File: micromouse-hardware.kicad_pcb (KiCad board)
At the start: 2 copper layers, 85 x 103.5 mm, 56 parts, among them J1 BATT-CONN, Q1 BCP56, Q10 BCP56, Q2 BCP56, Q3 BCP56, Q4 TEFT4300, Q5 TEFT4300, Q6 TEFT4300, Q7 TEFT4300, Q8 TEFT4300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

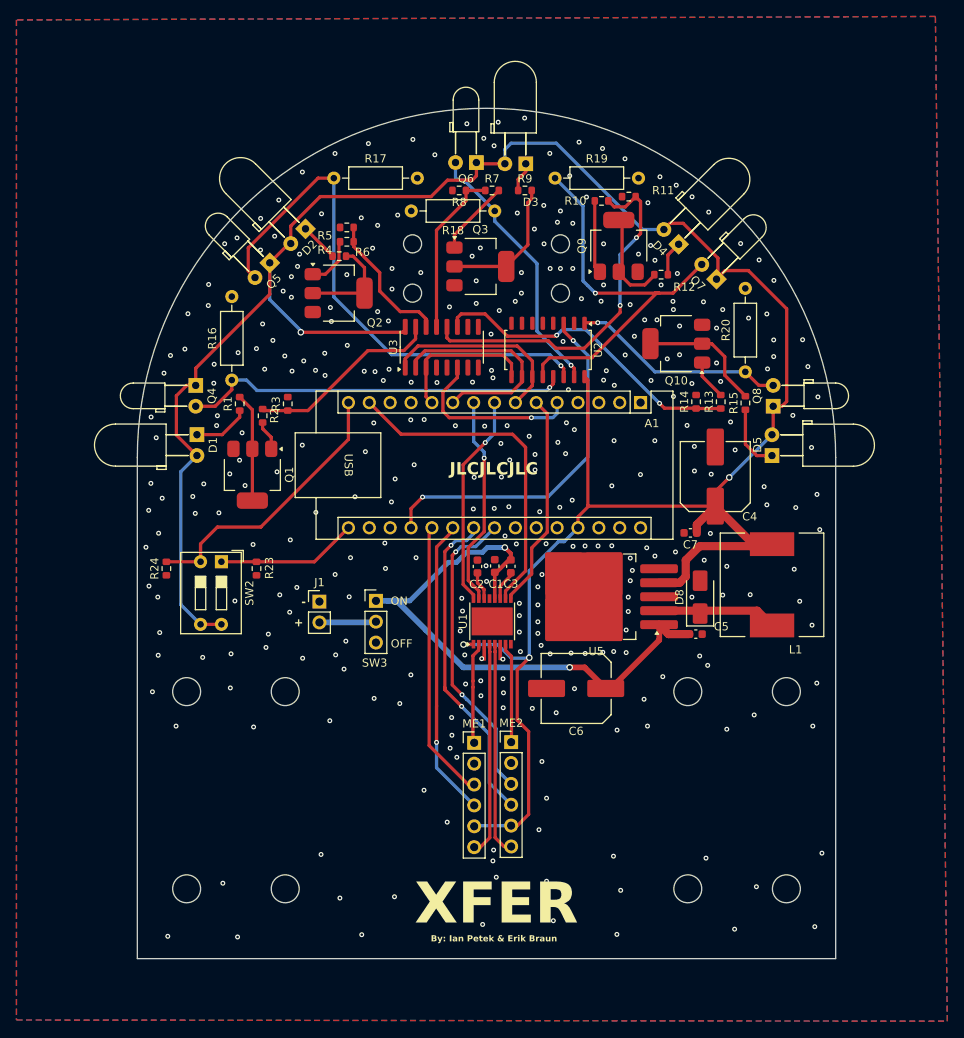
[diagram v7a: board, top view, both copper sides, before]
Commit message: promjenio tranistore u mosfete, jos neki popravci
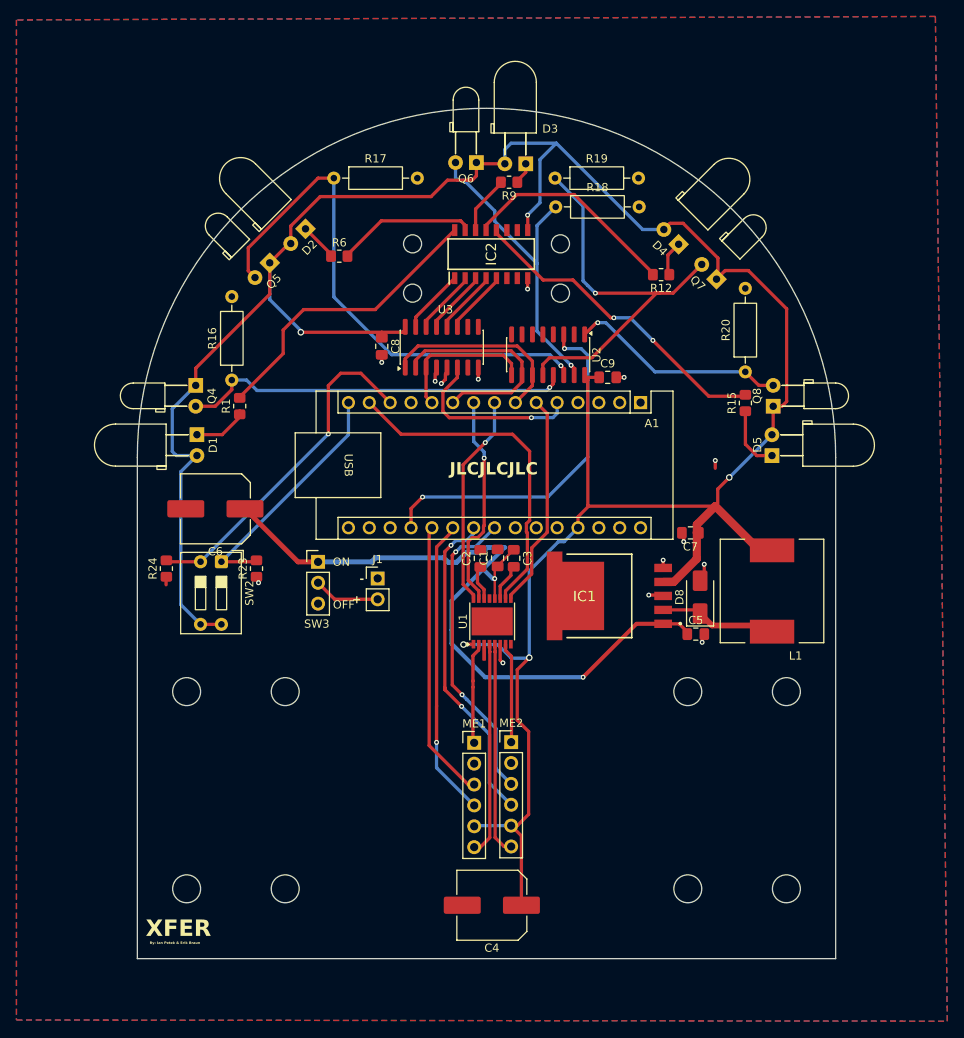
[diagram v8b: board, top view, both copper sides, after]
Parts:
- removed Q1, Q10, Q2, Q3, Q9: BCP56, Custom:SOT-223-3_TabPin4
- removed R10, R13, R2, R4, R7: 820R, Resistor_SMD:R_0603_1608Metric
- removed R11, R14, R3, R5, R8: 10K, Resistor_SMD:R_0603_1608Metric
- removed U5: LM2575GR-5.0, Package_TO_SOT_SMD:TO-263-5_TabPin3
- added C8: 100nF, Capacitor_SMD:C_0805_2012Metric_Pad1.18x1.45mm_HandSolder, F.Cu at (137.2, 73.5)
- added C9: 100nF, Capacitor_SMD:C_0805_2012Metric_Pad1.18x1.45mm_HandSolder, F.Cu at (164.8, 77.2)
- added IC1: LM2575SX-5.0_NOPB, Custom:KTT0005B, F.Cu at (159.0, 103.8)
- added IC2: TBD62003AFG,EL, Custom:SOIC127P630X190-16N, F.Cu at (150.6, 62.2)
- C1, C2, C3, C5, C7: footprint Capacitor_SMD:C_0603_1608Metric -> Capacitor_SMD:C_0805_2012Metric_Pad1.18x1.45mm_HandSolder
- D1, D2, D3, D4, D5: value SHF4545 -> SFH4545
- R1, R12, R15, R23, R24, R6, R9: footprint Resistor_SMD:R_0603_1608Metric -> Resistor_SMD:R_0805_2012Metric_Pad1.20x1.40mm_HandSolder
- U2: footprint Package_SO:SOIC-16_4.55x10.3mm_P1.27mm -> Package_SO:SOIC-16_3.9x9.9mm_P1.27mm
- moved C4 58.8 mm to (150.7, 141.5), turned to 180 degrees
- moved C6 49.1 mm to (117.0, 93.2)
- moved SW3 8.49 mm to (129.5, 99.7)
- moved J1 7.62 mm to (136.8, 101.7)
- moved R18 7.44 mm to (158.4, 56.5), turned to 0 degrees
- moved R9 2.17 mm to (152.8, 53.5), turned to 180 degrees
- moved C2 1.04 mm to (149.2, 99.3)
- moved C3 1.04 mm to (153.3, 99.3)
- moved C1 1.04 mm to (151.4, 99.2)
- moved L1 0.75 mm to (184.8, 103.2)
- moved U2 0.59 mm to (157.5, 74.5)
- moved R1 0.28 mm to (120.0, 80.8)
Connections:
- A1 pad 13: unconnected-(A1-D10-Pad13) -> Net-(A1-D10)
- A1 pad 16: Net-(A1-D13) -> unconnected-(A1-D13-Pad16)
- R23 pad 2: Net-(A1-D13) -> Net-(A1-D12)
- R24 pad 2: Net-(A1-D12) -> Net-(A1-D10)
- SW2 pad 1: Net-(A1-D13) -> Net-(A1-D12)
- SW2 pad 2: Net-(A1-D12) -> Net-(A1-D10)
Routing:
- net Net-(A1-D10): track 0.00 -> 41.7 mm, vias 0 -> 1
- net Net-(IC2-I4): track 43.9 -> 7.90 mm, vias 2 -> 0
- net Net-(IC2-I5): track 39.1 -> 7.90 mm, vias 2 -> 0
- net Net-(IC2-O5): track 15.5 -> 38.9 mm, vias 0 -> 2
- net Net-(IC2-O1): track 13.2 -> 36.3 mm
- net +VBAT: track 69.9 -> 92.7 mm
- net +5V: track 306.1 -> 324.2 mm, vias 4 -> 5
- net Net-(A1-D13): track 17.2 -> 0.00 mm
- net GND: track 0.00 -> 16.2 mm, vias 332 -> 14
- net Net-(IC2-I1): track 23.3 -> 7.90 mm
- net Net-(IC2-O4): track 11.3 -> 26.7 mm
- net Net-(IC2-I3): track 20.8 -> 7.90 mm
- net Net-(IC2-O3): track 16.8 -> 7.53 mm
- net Net-(Q3-B): track 9.19 -> 0.00 mm
- net Net-(Q9-B): track 8.89 -> 0.00 mm
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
